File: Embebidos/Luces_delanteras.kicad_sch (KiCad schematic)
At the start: 14 parts, among them J3 Pantallas I2C, J4 Luz_delantera, J5 Joystick, J6 RJ45, J7 RJ45, Q3 BSS138, Q4 DMP3056LSDQ-13

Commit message: Correccion Errores
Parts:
- removed J3: Pantallas I2C, symbol Connector:Conn_01x04_Female
- removed J4: Luz_delantera, symbol Connector:Conn_01x03_Female
- removed J5: Joystick, symbol Connector:Conn_01x08_Female
- removed J6: RJ45, symbol Connector:RJ45
- removed R4a1: 1k, symbol Device:R
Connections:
- no-connect marks 7 -> 3

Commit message: arreglos
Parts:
- added J3: Pantallas I2C, symbol Connector:Conn_01x04_Female
- added J4: Luz_delantera, symbol Connector:Conn_01x03_Female
- added J5: Joystick, symbol Connector:Conn_01x08_Female
- added J6: RJ45, symbol Connector:RJ45
- added R4a1: 1k, symbol Device:R
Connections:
- new net: J3.4 (Pin_4), J5.1 (Pin_1), J6.1, R4a1.1
- new net: J5.2 (Pin_2), J6.2
- new net: J5.4 (Pin_4), J6.3
- new net: J5.5 (Pin_5), J6.4
- new net: J4.3 (Pin_3), J6.5
- new net: J3.2 (Pin_2), J6.6
- new net: J3.1 (Pin_1), J6.7
- new net: J3.3 (Pin_3), J4.1 (Pin_1), J6.8
- new net: J4.2 (Pin_2), R4a1.2
- no-connect marks 3 -> 7

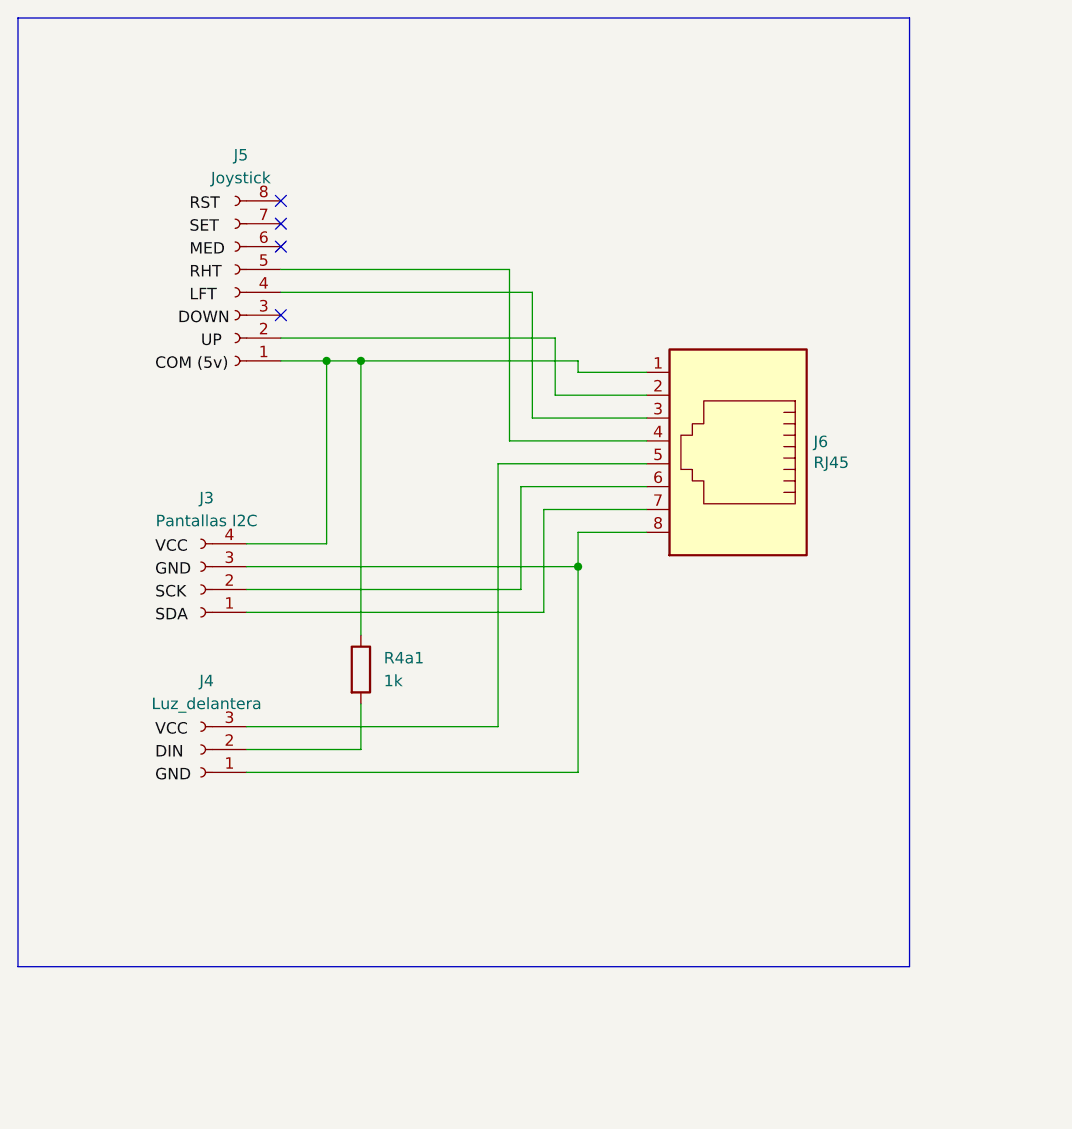
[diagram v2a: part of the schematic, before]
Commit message: Correccion errores y huellas leds LDR
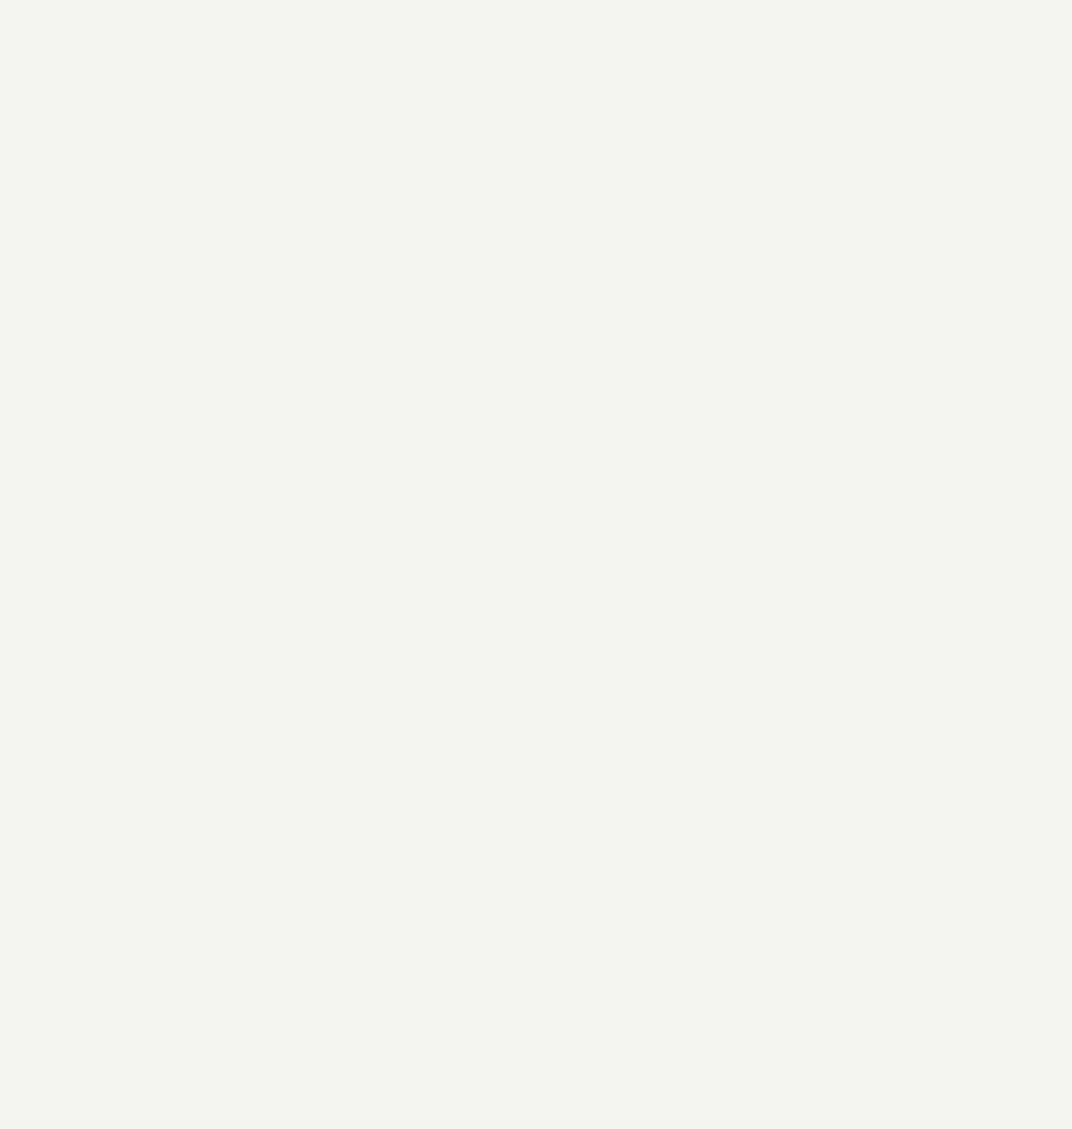
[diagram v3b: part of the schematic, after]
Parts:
- removed J3: Pantallas I2C, symbol Connector:Conn_01x04_Female
- removed J4: Luz_delantera, symbol Connector:Conn_01x03_Female
- removed J5: Joystick, symbol Connector:Conn_01x08_Female
- removed J6: RJ45, symbol Connector:RJ45
- removed R4a1: 1k, symbol Device:R
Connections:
- no-connect marks 7 -> 3

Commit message: Huellas
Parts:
- J7: footprint (none) -> Connector_RJ:RJ45_Amphenol_54602-x08_Horizontal
- R1a1, R22, R23, R24, R2a1, R3a1: footprint (none) -> Resistor_SMD:R_0805_2012Metric_Pad1.20x1.40mm_HandSolder
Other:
- note added: "Drain del transistor a al pin 5 RJ45."
- note removed: "Drain del transistor a al pin 5 RJ45"
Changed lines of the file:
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@@
     (stroke (width 0) (type default) (color 0 0 0 0))
   )
-  (text "Drain del transistor a \nal pin 5 RJ45\n" (at 261.62 86.36 0)
+  (text "Drain del transistor a \nal pin 5 RJ45.\n" (at 261.62 86.36 0)
     (effects (font (size 1.27 1.27)) (justify left bottom))
   )
@@
     (property "Reference" "J7" (id 0) (at 169.0878 77.0382 0))
     (property "Value" "RJ45" (id 1) (at 169.0878 79.3496 0))
-    (property "Footprint" "" (id 2) (at 167.64 93.345 90)
+    (property "Footprint" "Connector_RJ:RJ45_Amphenol_54602-x08_Horizontal" (id 2) (at 167.64 93.345 90)
       (effects (font (size 1.27 1.27)) hide)
     )
@@
     (property "Reference" "R1a1" (id 0) (at 198.12 101.6 90))
     (property "Value" "1K" (id 1) (at 198.12 104.14 90))
-    (property "Footprint" "" (id 2) (at 198.12 105.918 90)
+    (property "Footprint" "Resistor_SMD:R_0805_2012Metric_Pad1.20x1.40mm_HandSolder" (id 2) (at 198.12 105.918 90)
       (effects (font (size 1.27 1.27)) hide)
     )
@@
     (property "Reference" "R22" (id 0) (at 186.69 140.97 90))
     (property "Value" "1k" (id 1) (at 186.69 143.51 90))
-    (property "Footprint" "" (id 2) (at 186.69 145.288 90)
+    (property "Footprint" "Resistor_SMD:R_0805_2012Metric_Pad1.20x1.40mm_HandSolder" (id 2) (at 186.69 145.288 90)
       (effects (font (size 1.27 1.27)) hide)
     )
@@
     (property "Reference" "R23" (id 0) (at 190.5 149.86 90))
     (property "Value" "100k" (id 1) (at 193.04 149.86 90))
-    (property "Footprint" "" (id 2) (at 194.818 149.86 90)
+    (property "Footprint" "Resistor_SMD:R_0805_2012Metric_Pad1.20x1.40mm_HandSolder" (id 2) (at 194.818 149.86 90)
       (effects (font (size 1.27 1.27)) hide)
     )
@@
     (property "Reference" "R24" (id 0) (at 200.66 132.08 90))
     (property "Value" "100k" (id 1) (at 203.2 132.08 90))
-    (property "Footprint" "" (id 2) (at 204.978 132.08 90)
+    (property "Footprint" "Resistor_SMD:R_0805_2012Metric_Pad1.20x1.40mm_HandSolder" (id 2) (at 204.978 132.08 90)
       (effects (font (size 1.27 1.27)) hide)
     )
@@
     (property "Reference" "R2a1" (id 0) (at 207.01 96.52 90))
     (property "Value" "1K" (id 1) (at 207.01 99.06 90))
-    (property "Footprint" "" (id 2) (at 207.01 100.838 90)
+    (property "Footprint" "Resistor_SMD:R_0805_2012Metric_Pad1.20x1.40mm_HandSolder" (id 2) (at 207.01 100.838 90)
       (effects (font (size 1.27 1.27)) hide)
     )
@@
     (property "Reference" "R3a1" (id 0) (at 218.44 91.44 90))
     (property "Value" "1K" (id 1) (at 218.44 93.98 90))
-    (property "Footprint" "" (id 2) (at 218.44 95.758 90)
+    (property "Footprint" "Resistor_SMD:R_0805_2012Metric_Pad1.20x1.40mm_HandSolder" (id 2) (at 218.44 95.758 90)
       (effects (font (size 1.27 1.27)) hide)
     )

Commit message: Anotaciones
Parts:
- renumbered J7 to J3
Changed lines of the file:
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@@
   (symbol (lib_id "Connector:RJ45") (at 167.64 93.98 0) (unit 1)
     (in_bom yes) (on_board yes)
-    (property "Reference" "J7" (id 0) (at 169.0878 77.0382 0))
+    (property "Reference" "J3" (id 0) (at 169.0878 77.0382 0))
     (property "Value" "RJ45" (id 1) (at 169.0878 79.3496 0))
     (property "Footprint" "Connector_RJ:RJ45_Amphenol_54602-x08_Horizontal" (id 2) (at 167.64 93.345 90)
